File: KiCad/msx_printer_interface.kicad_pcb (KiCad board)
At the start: 2 copper layers, 65.7 x 54 mm, 11 parts, among them J1 MSX Cartridge Connector, J2 Conn_02x07_Top_Bottom, U1 ATF22V10C-15PU, U2 74HC273

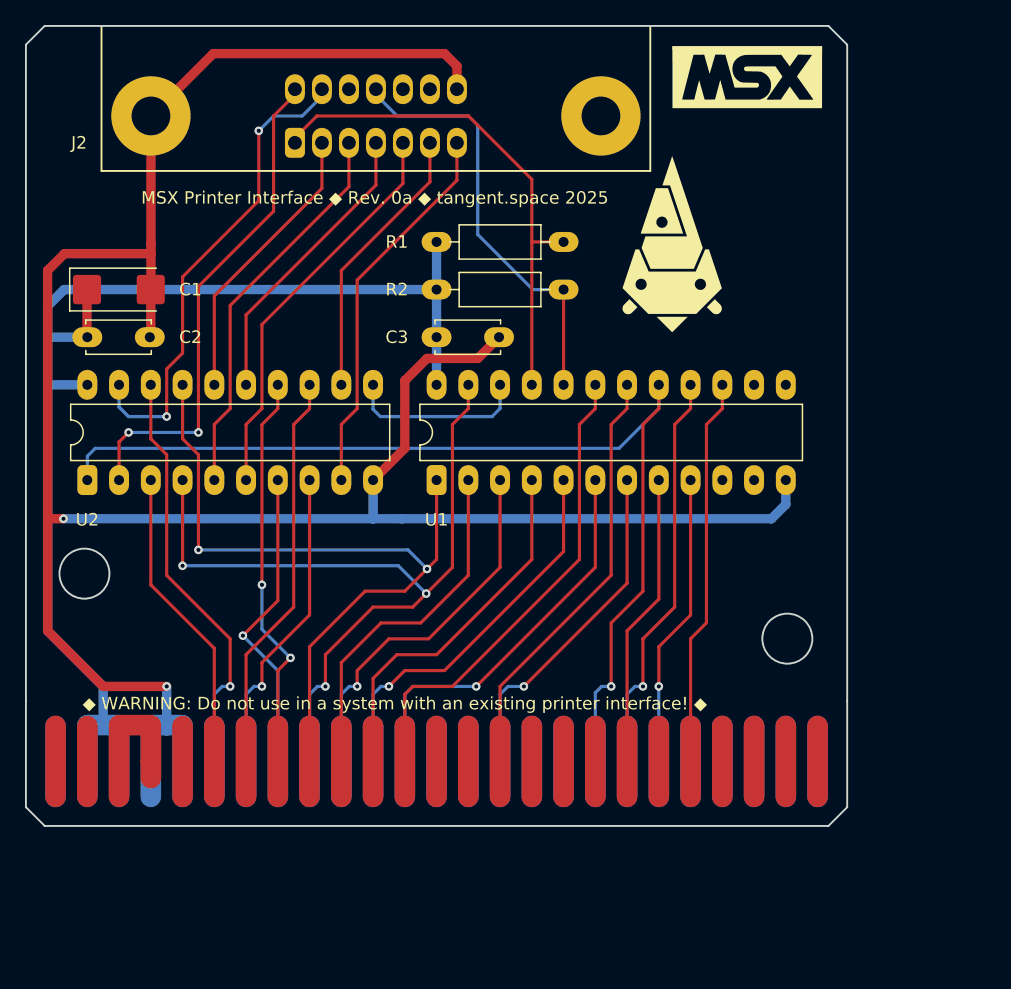
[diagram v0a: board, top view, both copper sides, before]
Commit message: Fix mounting holes(!), reduce pcb height 1mm
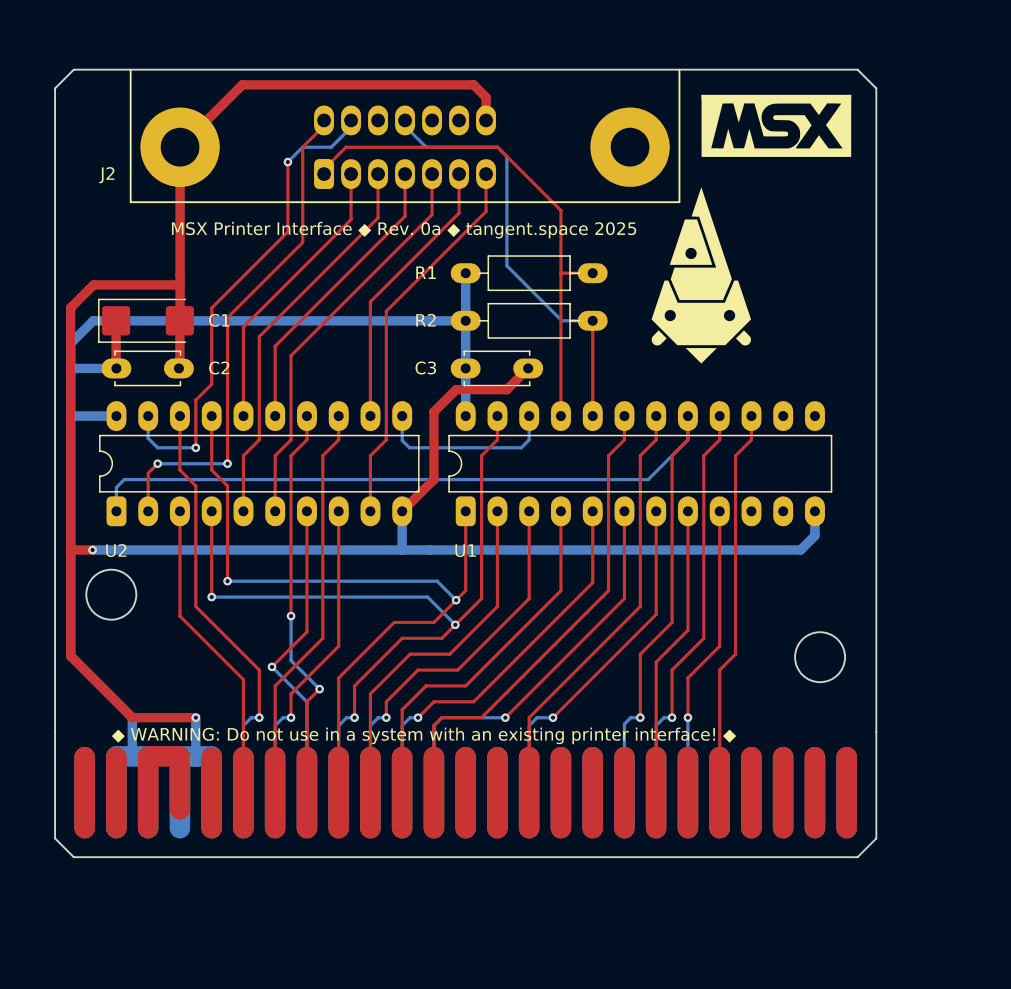
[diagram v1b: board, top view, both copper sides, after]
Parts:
- moved G*** 4.54 mm to (86.5, 11.5)
- moved J2 3.42 mm to (34.9, 2.50)
- moved C2 3.42 mm to (33.7, 30.9)
- moved U2 3.42 mm to (33.7, 42.3)
- moved J1 3.42 mm to (2.33, 2.50)
- moved C1 3.42 mm to (36.3, 27.1)
- moved C3 3.42 mm to (61.7, 30.9)
- moved G*** 3.42 mm to (80.5, 23.4)
- moved R1 3.42 mm to (71.8, 23.3)
- moved R2 3.42 mm to (71.8, 27.1)
- moved U1 3.42 mm to (61.7, 42.3)
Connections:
- J2 pad : (no net) -> GND
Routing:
- net Net-(J1-Pin_44): track 3.60 -> 2.54 mm
- net VCC: track 91.1 -> 92.0 mm
- net GND: track 183.6 -> 184.3 mm
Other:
- board size 65.7 x 54 mm -> 65.7 x 53 mm

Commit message: Add Centronics connector drawing
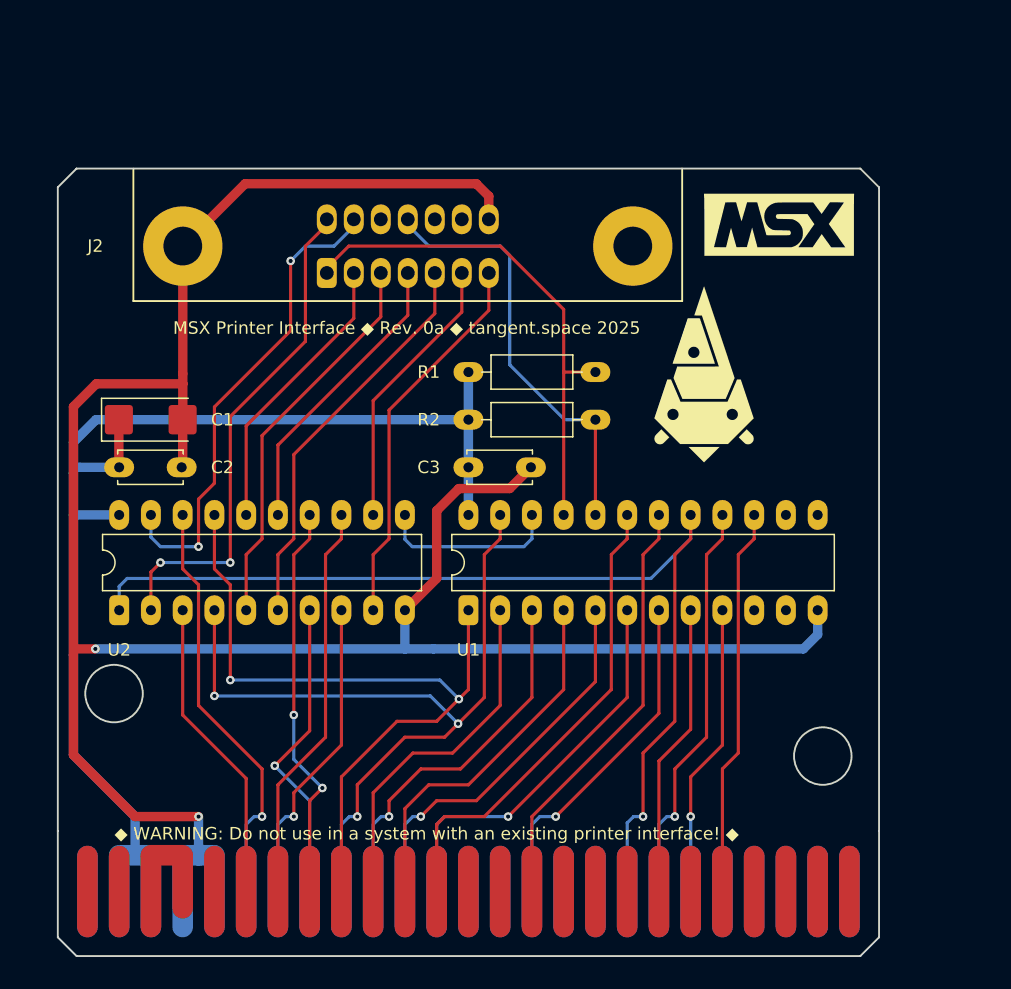
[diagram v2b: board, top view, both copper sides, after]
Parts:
- moved C2 7.91 mm to (34.0, 38.8)
- moved C3 7.91 mm to (61.9, 38.8)
- moved U1 7.91 mm to (61.9, 50.2)
- moved U2 7.91 mm to (34.0, 50.2)
- moved C1 7.91 mm to (36.5, 35.0)
- moved G*** 7.91 mm to (86.7, 19.4)
- moved G*** 7.91 mm to (80.7, 31.3)
- moved J1 7.91 mm to (2.55, 10.4)
- moved J2 7.91 mm to (35.1, 10.4)
- moved R1 7.91 mm to (72.1, 31.2)
- moved R2 7.91 mm to (72.1, 35.0)

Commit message: Update msx_printer_interface.kicad_pcb
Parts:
- moved C1 0.59 mm to (36.4, 35.6)
- moved R2 0.59 mm to (72.0, 35.6)
- moved G*** 0.59 mm to (86.7, 20.0)
- moved G*** 0.59 mm to (80.7, 31.9)
- moved J2 0.59 mm to (35.0, 11.0)
- moved J1 0.59 mm to (2.50, 11.0)
- moved R1 0.59 mm to (72.0, 31.8)
- moved C2 0.59 mm to (33.9, 39.4)
- moved U2 0.59 mm to (33.9, 50.8)
- moved C3 0.59 mm to (61.9, 39.4)
- moved U1 0.59 mm to (61.9, 50.8)
